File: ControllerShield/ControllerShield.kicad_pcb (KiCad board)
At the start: 2 copper layers, 68.6 x 53.3 mm, 11 parts, among them J1 Power, J2 Digital/PWM, J3 Analog, J4 Digital/PWM, U1 COM-09032, U2 LIS3DH, U3 LSF0102DQER

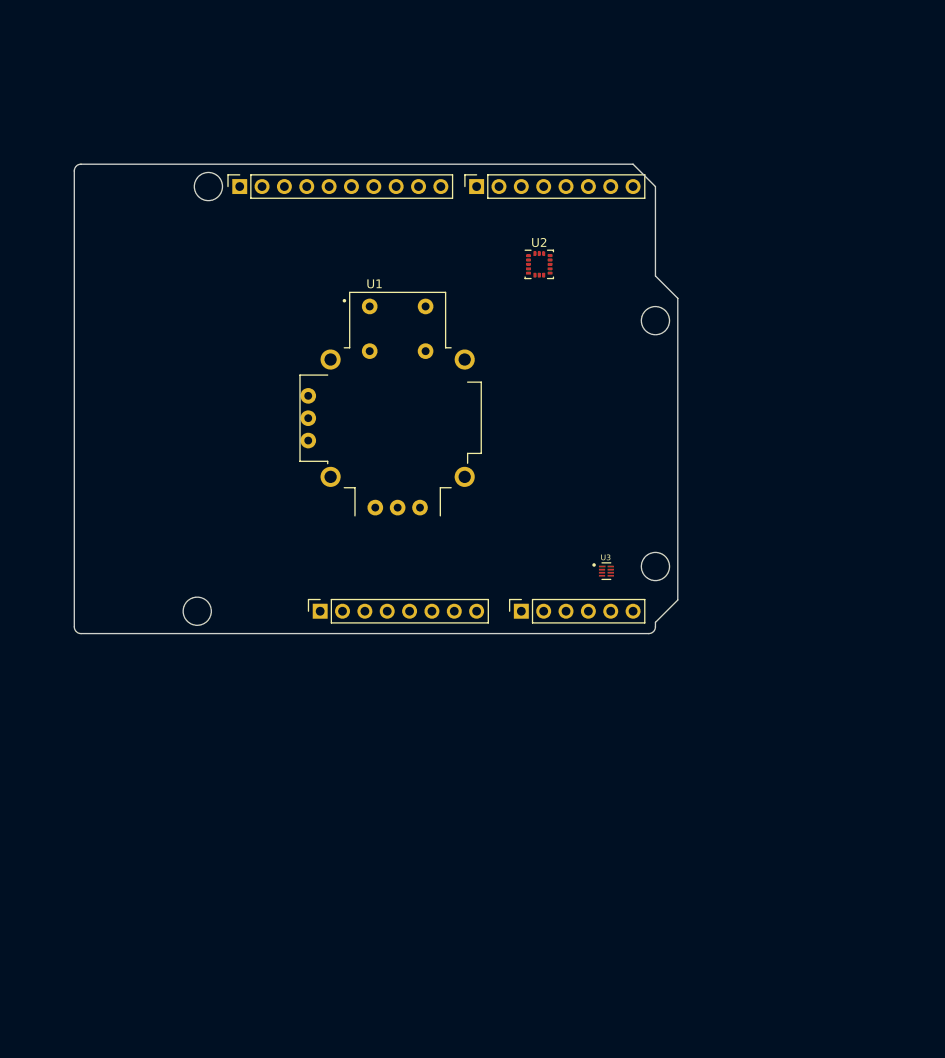
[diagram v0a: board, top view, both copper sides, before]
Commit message: Tweak the connector board a bit.  Rearrange X and Y.  May do more depending on the other board.
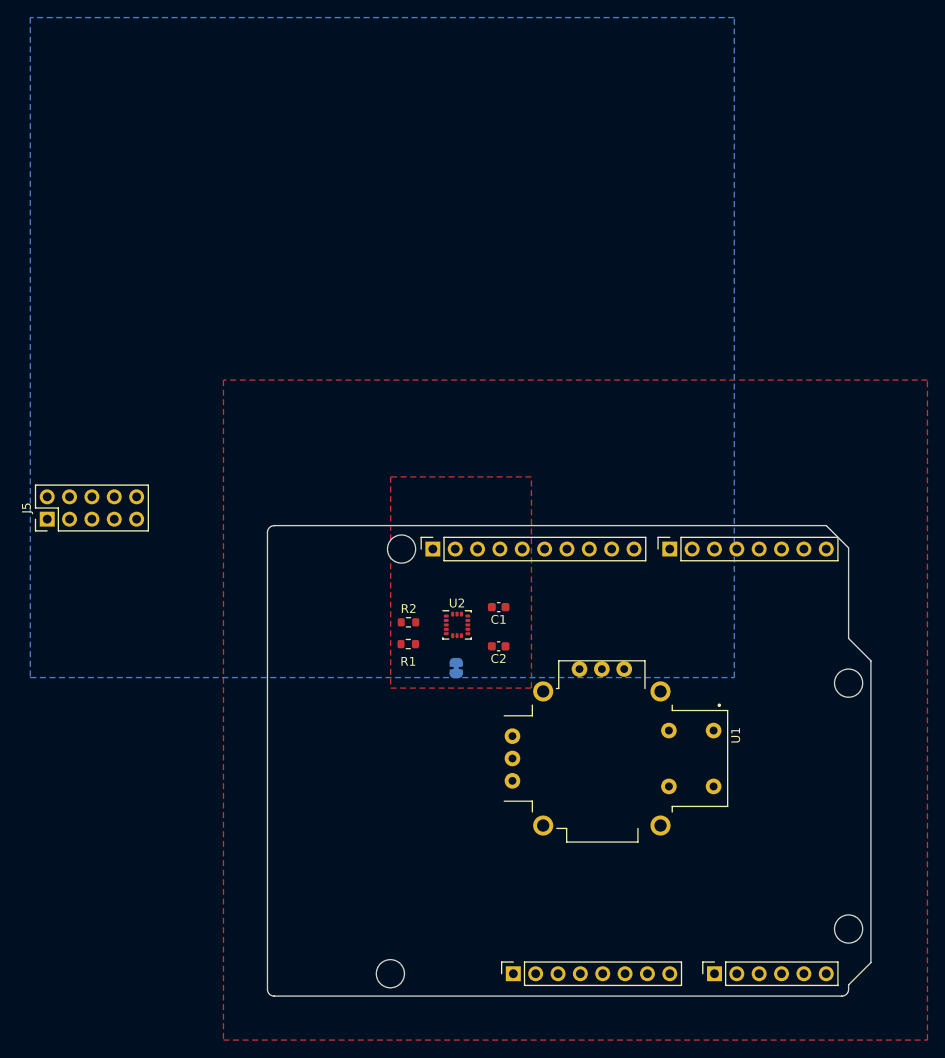
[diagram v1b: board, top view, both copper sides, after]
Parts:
- removed U3: LSF0102DQER, Footprints:SON35P140X100X40-8N
- added C1: 100nF, Capacitor_SMD:C_0603_1608Metric, F.Cu at (148.2, 97.0)
- added C2: 10uF, Capacitor_SMD:C_0603_1608Metric, F.Cu at (148.2, 101.4)
- added J5: Conn_02x05_Odd_Even, Connector_PinHeader_2.54mm:PinHeader_2x05_P2.54mm_Vertical, F.Cu at (96.9, 87.0)
- added JP1: SolderJumper_2_Bridged, Jumper:SolderJumper-2_P1.3mm_Bridged_RoundedPad1.0x1.5mm, B.Cu at (143.4, 103.9)
- added R1: 10K, Resistor_SMD:R_0603_1608Metric, F.Cu at (137.9, 101.2)
- added R2: 10K, Resistor_SMD:R_0603_1608Metric, F.Cu at (138.0, 98.7)
- moved MH3 46.7 mm to (188.0, 105.6)
- moved J1 46.7 mm to (149.9, 138.7)
- moved J3 46.7 mm to (172.8, 138.7)
- moved MH2 46.7 mm to (135.9, 138.7)
- moved MH4 46.7 mm to (188.0, 133.6)
- moved J2 46.7 mm to (140.7, 90.4)
- moved MH1 46.7 mm to (137.2, 90.4)
- moved J4 46.7 mm to (167.7, 90.4)
- moved U1 45.1 mm to (159.9, 114.2), turned to -90 degrees
- moved U2 42.0 mm to (143.5, 99.0)
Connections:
- J1 pad 8: VCC -> /Vin
- J2 pad 1: /SCL/A5 -> /SCL
- J2 pad 2: /SDA/A4 -> /SDA
- J2 pad 8: /*10 -> /Y
- J2 pad 9: /*9 -> /X
- J3 pad 5: /SDA/A4 -> unconnected-(J3-Pin_5-Pad5)
- J3 pad 6: /SCL/A5 -> unconnected-(J3-Pin_6-Pad6)
- U1 pad B1A: unconnected-(U1-SEL+-PadB1A) -> /13
- U1 pad B2A: unconnected-(U1-SEL--PadB2A) -> GND
- U1 pad H1: unconnected-(U1-H+-PadH1) -> +5V
- U1 pad H2: unconnected-(U1-H-PadH2) -> /A1
- U1 pad H3: unconnected-(U1-H--PadH3) -> GND
- U1 pad S1: unconnected-(U1-SHIELD-PadS1) -> GND
- U1 pad S2: unconnected-(U1-SHIELD__1-PadS2) -> GND
- U1 pad S3: unconnected-(U1-SHIELD__2-PadS3) -> GND
- U1 pad S4: unconnected-(U1-SHIELD__3-PadS4) -> GND
- U1 pad V1: unconnected-(U1-V+-PadV1) -> +5V
- U1 pad V2: unconnected-(U1-V-PadV2) -> /A0
- U1 pad V3: unconnected-(U1-V--PadV3) -> GND
- U2 pad 1: unconnected-(U2-VDD_IO-Pad1) -> +3V3
- U2 pad 10: Net-(U2-GND-Pad10) -> GND
- U2 pad 12: Net-(U2-GND-Pad10) -> GND
- U2 pad 14: unconnected-(U2-VDD-Pad14) -> +3V3
- U2 pad 4: unconnected-(U2-SCL/SPC-Pad4) -> /SCL
- U2 pad 5: Net-(U2-GND-Pad10) -> GND
- U2 pad 6: unconnected-(U2-SDA/SDI/SDO-Pad6) -> /SDA
- U2 pad 7: unconnected-(U2-SDO/SA0-Pad7) -> Net-(JP1-B)
- U2 pad 8: unconnected-(U2-CS-Pad8) -> +3V3
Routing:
- added copper zone on F.Cu, net +3V3
- added copper zone on F.Cu, net +5V
- added copper zone on In1.Cu, net +5V
- added copper zone on B.Cu, net GND
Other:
- board size 68.6 x 53.3 mm -> 68.6 x 53.5 mm
- copper layers 2 -> 4

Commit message: work on controller
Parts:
- moved J5 38.0 mm to (127.2, 109.9), turned to 0 degrees
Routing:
- net /SCL: track 0.00 -> 12.9 mm
- net /SDA: track 0.00 -> 4.62 mm
- net GND: track 0.00 -> 1.12 mm, vias 0 -> 1
- added copper zone on F.Cu, net /Vin
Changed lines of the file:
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@@
   )
   (footprint "Connector_PinHeader_2.54mm:PinHeader_2x05_P2.54mm_Vertical" (layer "F.Cu")
-    (at 96.92 87 90)
+    (at 127.21 109.92)
     (descr "Through hole straight pin header, 2x05, 2.54mm pitch, double rows")
     (tags "Through hole pin header THT 2x05 2.54mm double row")
@@
     (property "ki_keywords" "connector")
     (attr through_hole)
-    (fp_text reference "J5" (at 1.27 -2.33 90) (layer "F.SilkS")
-        (effects (font (size 1 1) (thickness 0.15)))
-    )
-    (fp_text value "Conn_02x05_Odd_Even" (at 1.27 12.49 90) (layer "F.Fab") hide
-        (effects (font (size 1 1) (thickness 0.15)))
-    )
-    (fp_text user "${REFERENCE}" (at 1.27 5.08) (layer "F.Fab")
+    (fp_text reference "J5" (at 1.27 -2.33) (layer "F.SilkS")
+        (effects (font (size 1 1) (thickness 0.15)))
+    )
+    (fp_text value "Conn_02x05_Odd_Even" (at 1.27 12.49) (layer "F.Fab") hide
+        (effects (font (size 1 1) (thickness 0.15)))
+    )
+    (fp_text user "${REFERENCE}" (at 1.27 5.08 90) (layer "F.Fab")
         (effects (font (size 1 1) (thickness 0.15)))
     )
@@
     (fp_line (start 3.81 11.43) (end -1.27 11.43)
       (stroke (width 0.1) (type solid)) (layer "F.Fab"))
-    (pad "1" thru_hole rect (at 0 0 90) (size 1.7 1.7) (drill 1) (layers "*.Cu" "*.Mask")
+    (pad "1" thru_hole rect (at 0 0) (size 1.7 1.7) (drill 1) (layers "*.Cu" "*.Mask")
       (net 32 "unconnected-(J5-Pin_1-Pad1)") (pinfunction "Pin_1") (pintype "passive+no_connect"))
-    (pad "2" thru_hole oval (at 2.54 0 90) (size 1.7 1.7) (drill 1) (layers "*.Cu" "*.Mask")
+    (pad "2" thru_hole oval (at 2.54 0) (size 1.7 1.7) (drill 1) (layers "*.Cu" "*.Mask")
       (net 17 "unconnected-(J5-Pin_2-Pad2)") (pinfunction "Pin_2") (pintype "passive+no_connect"))
-    (pad "3" thru_hole oval (at 0 2.54 90) (size 1.7 1.7) (drill 1) (layers "*.Cu" "*.Mask")
+    (pad "3" thru_hole oval (at 0 2.54) (size 1.7 1.7) (drill 1) (layers "*.Cu" "*.Mask")
       (net 40 "/X") (pinfunction "Pin_3") (pintype "passive"))
-    (pad "4" thru_hole oval (at 2.54 2.54 90) (size 1.7 1.7) (drill 1) (layers "*.Cu" "*.Mask")
+    (pad "4" thru_hole oval (at 2.54 2.54) (size 1.7 1.7) (drill 1) (layers "*.Cu" "*.Mask")
       (net 18 "unconnected-(J5-Pin_4-Pad4)") (pinfunction "Pin_4") (pintype "passive+no_connect"))
-    (pad "5" thru_hole oval (at 0 5.08 90) (size 1.7 1.7) (drill 1) (layers "*.Cu" "*.Mask")
+    (pad "5" thru_hole oval (at 0 5.08) (size 1.7 1.7) (drill 1) (layers "*.Cu" "*.Mask")
       (net 35 "/Y") (pinfunction "Pin_5") (pintype "passive"))
-    (pad "6" thru_hole oval (at 2.54 5.08 90) (size 1.7 1.7) (drill 1) (layers "*.Cu" "*.Mask")
+    (pad "6" thru_hole oval (at 2.54 5.08) (size 1.7 1.7) (drill 1) (layers "*.Cu" "*.Mask")
       (net 27 "unconnected-(J5-Pin_6-Pad6)") (pinfunction "Pin_6") (pintype "passive+no_connect"))
-    (pad "7" thru_hole oval (at 0 7.62 90) (size 1.7 1.7) (drill 1) (layers "*.Cu" "*.Mask")
+    (pad "7" thru_hole oval (at 0 7.62) (size 1.7 1.7) (drill 1) (layers "*.Cu" "*.Mask")
       (net 9 "/Vin") (pinfunction "Pin_7") (pintype "passive"))
-    (pad "8" thru_hole oval (at 2.54 7.62 90) (size 1.7 1.7) (drill 1) (layers "*.Cu" "*.Mask")
+    (pad "8" thru_hole oval (at 2.54 7.62) (size 1.7 1.7) (drill 1) (layers "*.Cu" "*.Mask")
       (net 33 "unconnected-(J5-Pin_8-Pad8)") (pinfunction "Pin_8") (pintype "passive+no_connect"))
-    (pad "9" thru_hole oval (at 0 10.16 90) (size 1.7 1.7) (drill 1) (layers "*.Cu" "*.Mask")
+    (pad "9" thru_hole oval (at 0 10.16) (size 1.7 1.7) (drill 1) (layers "*.Cu" "*.Mask")
       (net 1 "GND") (pinfunction "Pin_9") (pintype "passive"))
-    (pad "10" thru_hole oval (at 2.54 10.16 90) (size 1.7 1.7) (drill 1) (layers "*.Cu" "*.Mask")
+    (pad "10" thru_hole oval (at 2.54 10.16) (size 1.7 1.7) (drill 1) (layers "*.Cu" "*.Mask")
       (net 43 "unconnected-(J5-Pin_10-Pad10)") (pinfunction "Pin_10") (pintype "passive+no_connect"))
     (model "${KICAD6_3DMODEL_DIR}/Connector_PinHeader_2.54mm.3dshapes/PinHeader_2x05_P2.54mm_Vertical.wrl" hide
@@
     (effects (font (size 1 1) (thickness 0.15)))
   )
+  (segment (start 141.485 100.015) (end 141.25 100.25) (width 0.1778) (layer "F.Cu") (net 1))
+  (segment (start 142.27 100.015) (end 141.485 100.015) (width 0.1778) (layer "F.Cu") (net 1))
+  (via (at 141.25 100.25) (size 0.45) (drill 0.3) (layers "F.Cu" "B.Cu") (net 1))
+  (segment (start 142.27 99.515) (end 139.595 99.515) (width 0.1778) (layer "F.Cu") (net 10))
+  (segment (start 140.746 96.774) (end 138.8 98.72) (width 0.1778) (layer "F.Cu") (net 10))
+  (segment (start 139.595 99.515) (end 138.8 98.72) (width 0.1778) (layer "F.Cu") (net 10))
+  (segment (start 140.746 90.395) (end 140.746 96.774) (width 0.1778) (layer "F.Cu") (net 10))
+  (segment (start 142.995 100.24) (end 142.04 101.195) (width 0.1778) (layer "F.Cu") (net 29))
+  (segment (start 142.04 101.195) (end 138.775 101.195) (width 0.1778) (layer "F.Cu") (net 29))
+  (zone (net 9) (net_name "/Vin") (layer "F.Cu") (hatch edge 0.5)
+    (priority 4)
+    (connect_pads (clearance 0.25))
+    (min_thickness 0.25) (filled_areas_thickness no)
+    (fill yes (thermal_gap 0.5) (thermal_bridge_width 0.5))
+    (polygon
+      (pts
+        (xy 125 116.25)
+        (xy 131.75 116.25)
+        (xy 147.5 136.75)
+        (xy 170 136.75)
+        (xy 170 141.25)
+        (xy 146 141.25)
+        (xy 125 123.75)
+      )
+    )
+  )
   (zone (net 26) (net_name "+3V3") (layer "F.Cu") (hatch edge 0.5)
     (priority 2)
     (connect_pads (clearance 0.25))
     (min_thickness 0.25) (filled_areas_thickness no)
-    (fill (thermal_gap 0.5) (thermal_bridge_width 0.5))
+    (fill yes (thermal_gap 0.5) (thermal_bridge_width 0.5))
     (polygon
       (pts
@@
         (xy 151.95 82.195)
         (xy 135.95 82.195)
-        (xy 135.95 106.195)
       )
     )
@@
     (connect_pads (clearance 0.508))
     (min_thickness 0.25) (filled_areas_thickness no)
-    (fill (thermal_gap 0.5) (thermal_bridge_width 0.5))
+    (fill yes (thermal_gap 0.5) (thermal_bridge_width 0.5))
     (polygon
       (pts
@@
     (connect_pads (clearance 0.25))
     (min_thickness 0.25) (filled_areas_thickness no)
-    (fill (thermal_gap 0.5) (thermal_bridge_width 0.5))
+    (fill yes (thermal_gap 0.5) (thermal_bridge_width 0.5))
     (polygon
       (pts
@@
     (connect_pads (clearance 0.508))
     (min_thickness 0.25) (filled_areas_thickness no)
-    (fill (thermal_gap 0.5) (thermal_bridge_width 0.5))
+    (fill yes (thermal_gap 0.5) (thermal_bridge_width 0.5))
     (polygon
       (pts
-        (xy 95 30)
-        (xy 95 105)
-        (xy 175 105)
-        (xy 175 30)
-      )
-    )
+        (xy 116.5 71.25)
+        (xy 116.5 146.25)
+        (xy 196.5 146.25)
+        (xy 196.5 71.25)
+      )
+    )

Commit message: work on controller
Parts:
- added D1: RED, LED_THT:LED_D5.0mm, F.Cu at (128.0, 131.8)
- added D2: Green, LED_THT:LED_D5.0mm, F.Cu at (128.0, 96.8)
- added R3: 1K, Resistor_SMD:R_0603_1608Metric, F.Cu at (131.4, 138.0)
- added R4: 1K, Resistor_SMD:R_0603_1608Metric, F.Cu at (131.9, 91.8)
- added U3: TLV75533PDBV, Package_TO_SOT_SMD:SOT-23-5, F.Cu at (152.2, 97.5)
- C1: value 100nF -> 0.1uF
- moved C1 0.86 mm to (147.5, 96.5)
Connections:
- net /A0 renamed /Horiz
- net /A1 renamed /Vert
- net /Vin renamed /Vsys
- J1 pad 4: +3V3 -> unconnected-(J1-Pin_4-Pad4)
- J2 pad 5: /13 -> /D0
- J2 pad 6: /12 -> /D1
- J4 pad 4: /4 -> /Green
- J4 pad 5: /*3 -> /Red
- J4 pad 6: /2 -> /GameBtn
- J5 pad 1: unconnected-(J5-Pin_1-Pad1) -> /X
- J5 pad 2: unconnected-(J5-Pin_2-Pad2) -> /Y
- J5 pad 3: /X -> /SCL
- J5 pad 4: unconnected-(J5-Pin_4-Pad4) -> /SDA
- J5 pad 5: /Y -> /D0
- J5 pad 6: unconnected-(J5-Pin_6-Pad6) -> /D1
- U1 pad B1A: /13 -> /GameBtn
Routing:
- net /Red: track 0.00 -> 70.6 mm
- net /D0: track 0.00 -> 47.6 mm
- net /X: track 0.00 -> 44.5 mm
- net /Horiz: track 0.00 -> 39.9 mm
- net /Vert: track 0.00 -> 38.8 mm
- net /Y: track 0.00 -> 36.9 mm
- net /SDA: track 4.62 -> 41.5 mm, vias 0 -> 1
- net /D1: track 0.00 -> 34.4 mm
- net /SCL: track 12.9 -> 41.7 mm
- net /GameBtn: track 0.00 -> 23.8 mm
- net GND: track 1.12 -> 7.13 mm, vias 1 -> 5
- net Net-(JP1-B): track 0.00 -> 5.30 mm
- net /Vsys: track 0.00 -> 1.64 mm
- net +5V: vias 0 -> 1
- added copper zone on In2.Cu, net +5V

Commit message: Possible release candidate for Controller Board.
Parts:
- moved R3 36.6 mm to (134.0, 101.5), turned to -90 degrees
- moved R4 5.48 mm to (134.0, 96.8), turned to -90 degrees
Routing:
- net /Green: track 0.00 -> 44.1 mm
- net Net-(D1-A): track 0.00 -> 30.9 mm, vias 0 -> 1
- net /Red: track 70.6 -> 50.4 mm
- net /D1: track 34.4 -> 53.9 mm, vias 0 -> 1
- net /Y: track 36.9 -> 55.5 mm, vias 0 -> 1
- net +5V: track 0.00 -> 10.4 mm, vias 1 -> 3
- net /X: track 44.5 -> 51.9 mm, vias 0 -> 1
- net Net-(D2-A): track 0.00 -> 3.83 mm
- net /D0: track 47.6 -> 51.0 mm, vias 0 -> 1
- net Net-(JP1-B): track 5.30 -> 3.07 mm, vias 0 -> 1
- net /SCL: track 41.7 -> 40.4 mm, vias 0 -> 2
- net +3V3: track 0.00 -> 1.03 mm
- net /Vsys: track 1.64 -> 2.50 mm
- net GND: track 7.13 -> 7.68 mm, vias 5 -> 6
- net /Vert: track 38.8 -> 39.3 mm
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- removed copper zone on In1.Cu, net +5V
- removed copper zone on In2.Cu, net +5V
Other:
- copper layers 4 -> 2

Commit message: Add switch to controller
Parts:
- added SW1: Small Switch TH, Footprints:SW4_1825910-B_TEC, F.Cu at (182.5, 133.8)
- U2: value LIS3DH -> LIS2DE12TR
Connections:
- J1 pad 3: /~{RESET} -> /RSTn
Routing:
- net /RSTn: track 0.00 -> 34.1 mm
- net GND: track 7.68 -> 11.5 mm
- net +3V3: track 1.03 -> 3.43 mm
- net +5V: track 10.4 -> 12.3 mm

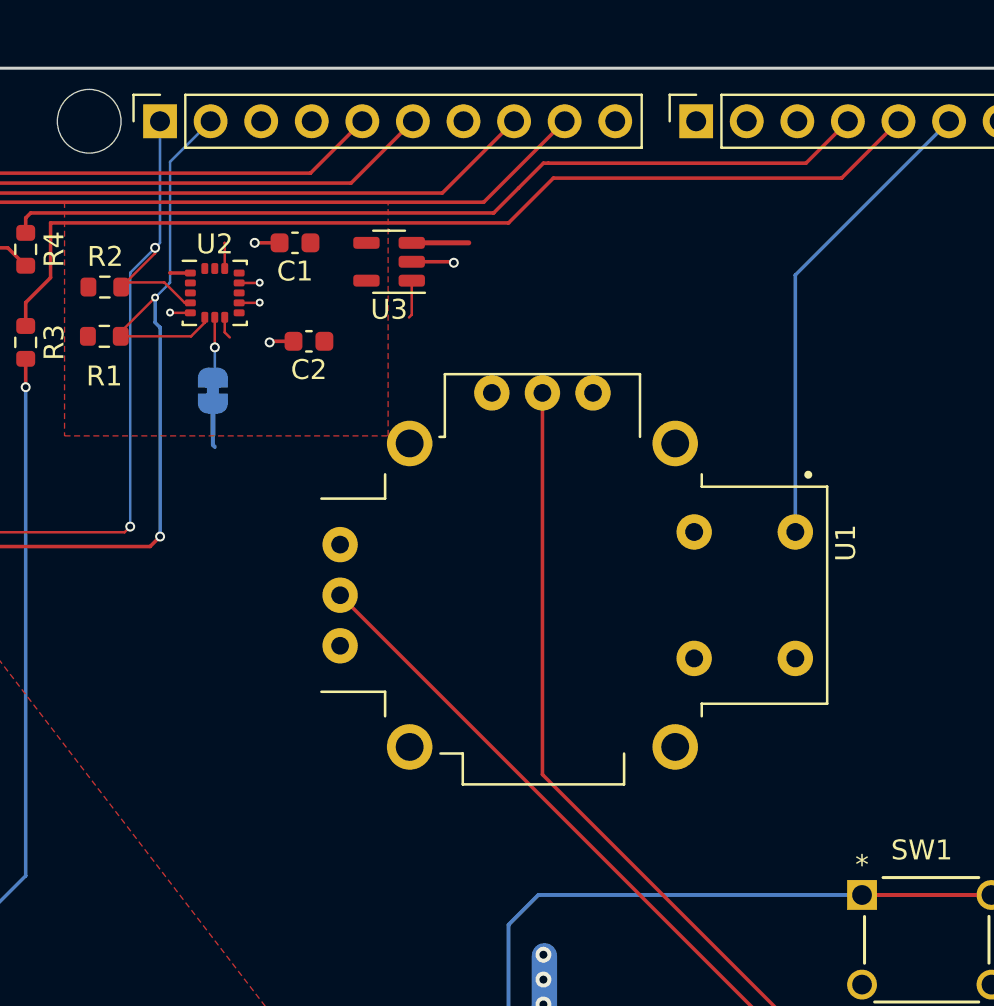
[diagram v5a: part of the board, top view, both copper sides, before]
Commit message: add probe points
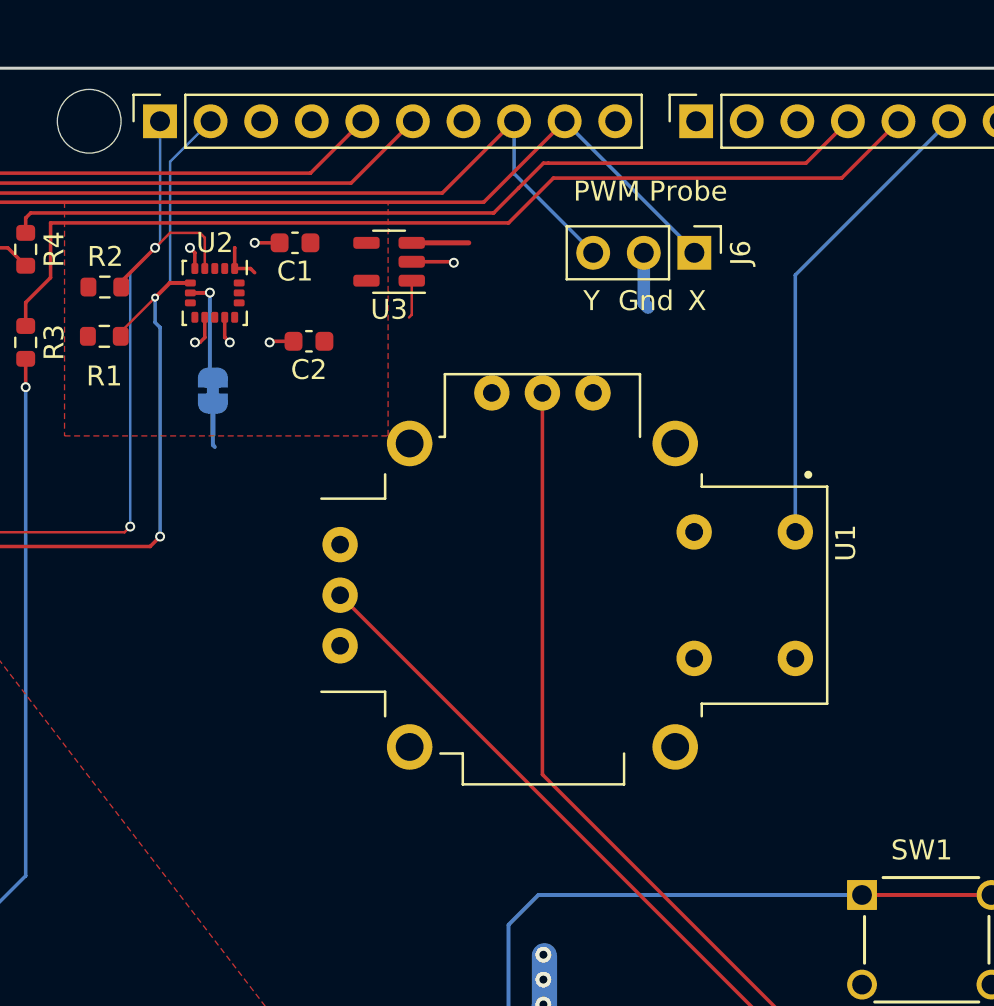
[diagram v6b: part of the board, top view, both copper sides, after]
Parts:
- added J6: Debug Point, Connector_PinHeader_2.54mm:PinHeader_1x03_P2.54mm_Vertical, F.Cu at (167.6, 97.0)
- U2: value LIS2DE12TR -> LIS3DHTR
- turned U2 to -90 degrees
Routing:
- net /X: track 51.9 -> 61.2 mm
- net /Y: track 55.5 -> 63.8 mm
- net GND: track 11.5 -> 15.4 mm
- net /SDA: track 41.0 -> 38.3 mm
- net Net-(JP1-B): track 3.07 -> 5.32 mm
- net +3V3: track 3.43 -> 2.13 mm
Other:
- board text added: "Gnd"
- board text added: "PWM Probe"
- board text added: "X"
- board text added: "Y"

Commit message: Release candidate for controller board
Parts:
- added G***: LOGO, QRCodes:v0.6cb, F.Cu at (140.2, 125.8)
